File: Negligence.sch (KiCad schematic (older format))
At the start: 116 parts, among them J1 AVR-ISP-6, SW1 keyboard_parts_KEYSW, SW10 keyboard_parts_KEYSW, SW11 keyboard_parts_KEYSW, SW12 keyboard_parts_KEYSW, SW13 keyboard_parts_KEYSW, SW14 keyboard_parts_KEYSW, SW15 keyboard_parts_KEYSW, SW16 keyboard_parts_KEYSW, SW17 keyboard_parts_KEYSW, SW18 keyboard_parts_KEYSW, SW19 keyboard_parts_KEYSW, SW2 keyboard_parts_KEYSW, SW20 keyboard_parts_KEYSW, SW21 keyboard_parts_KEYSW, SW22 keyboard_parts_KEYSW, SW23 keyboard_parts_KEYSW, SW24 keyboard_parts_KEYSW, SW25 keyboard_parts_KEYSW, SW26 keyboard_parts_KEYSW, SW27 keyboard_parts_KEYSW, SW28 keyboard_parts_KEYSW, SW29 keyboard_parts_KEYSW, SW3 keyboard_parts_KEYSW, SW30 keyboard_parts_KEYSW, SW31 keyboard_parts_KEYSW, SW32 keyboard_parts_KEYSW, SW33 keyboard_parts_KEYSW, SW34 keyboard_parts_KEYSW, SW35 keyboard_parts_KEYSW, SW36 keyboard_parts_KEYSW, SW37 keyboard_parts_KEYSW, SW38 keyboard_parts_KEYSW, SW39 keyboard_parts_KEYSW, SW4 keyboard_parts_KEYSW, SW40 keyboard_parts_KEYSW, SW41 keyboard_parts_KEYSW, SW42 keyboard_parts_KEYSW, SW43 keyboard_parts_KEYSW, SW44 keyboard_parts_KEYSW, SW45 keyboard_parts_KEYSW, SW46 keyboard_parts_KEYSW, SW47 RESET, SW48 BOOT, SW5 keyboard_parts_KEYSW, SW6 keyboard_parts_KEYSW, SW7 keyboard_parts_KEYSW, SW8 keyboard_parts_KEYSW, SW9 keyboard_parts_KEYSW, U1 ATmega328P-PU, Y1 16MHz

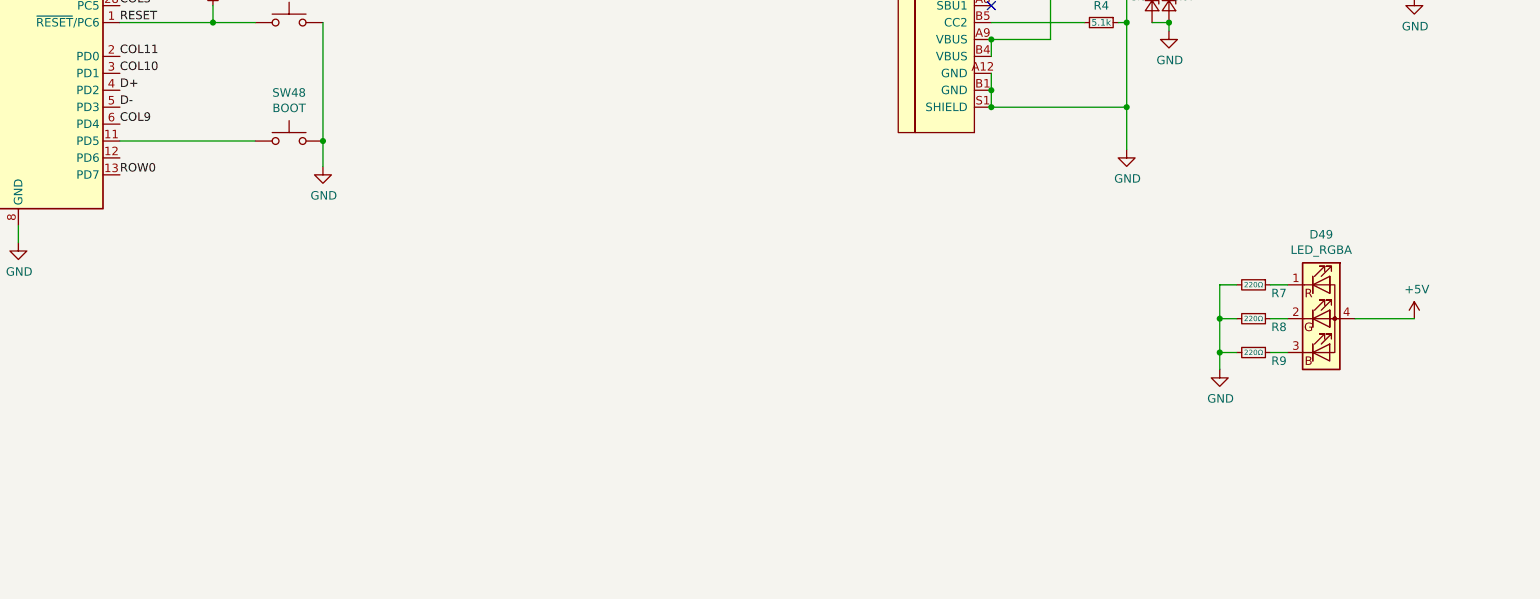
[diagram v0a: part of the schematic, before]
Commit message: Add addressable led
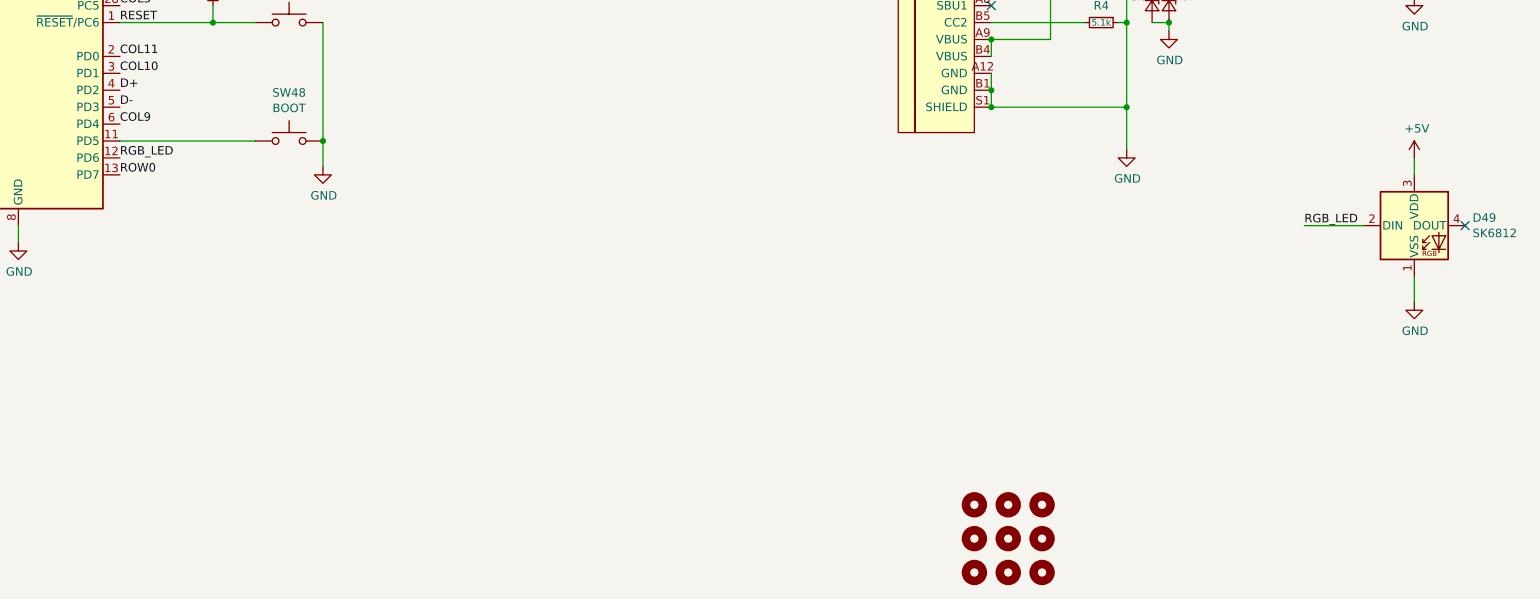
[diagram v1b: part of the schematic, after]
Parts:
- removed D49: LED_RGBA, LED_THT:LED_D5.0mm-4_RGB, symbol Device:LED_RGBA
- removed R7, R8, R9: 220Ω, cftkb:R_Axial_DIN0204_L3.6mm_D1.6mm_P7.62mm_Horizontal, symbol Device:R_Small
- added D49: SK6812, LED_SMD:LED_SK6812_PLCC4_5.0x5.0mm_P3.2mm, symbol LED:SK6812
- added H1, H2, H3, H4, H5, H6, H7, H8, H9: MountingHole, MountingHole:MountingHole_2.2mm_M2, symbol Mechanical:MountingHole
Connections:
- net +5V: now also D49.3 (VDD)
- net GND: now also D49.1 (VSS)
- net RGB_LED: now reaches U1.12 (PD6)
- net RGB_LED: now also D49.2 (DIN)
- no-connect marks 3 -> 4
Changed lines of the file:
@@
 Text Label 6900 7450 0    50   ~ 0
 ROW0
+Text Label 13900 7750 0    50   ~ 0
+RGB_LED
+Wire Wire Line
+	13900 7750 14250 7750
 $Comp
-L power:+5V #PWR016
-U 1 1 5F6FE958
-P 14550 8300
-F 0 "#PWR016" H 14550 8150 50  0001 C CNN
-F 1 "+5V" H 14565 8473 50  0000 C CNN
-F 2 "" H 14550 8300 50  0001 C CNN
-F 3 "" H 14550 8300 50  0001 C CNN
-	1    14550 8300
+L power:GND #PWR016
+U 1 1 5DEC76FA
+P 14550 8200
+F 0 "#PWR016" H 14550 7950 50  0001 C CNN
+F 1 "GND" H 14555 8027 50  0000 C CNN
+F 2 "" H 14550 8200 50  0001 C CNN
+F 3 "" H 14550 8200 50  0001 C CNN
+	1    14550 8200
 	1    0    0    -1
 $EndComp
 Wire Wire Line
-	14200 8300 14550 8300
+	14550 8050 14550 8200
+NoConn ~ 14850 7750
+Text Label 6900 7350 0    50   ~ 0
+RGB_LED
 $Comp
-L Device:R_Small R9
-U 1 1 5F717CE0
-P 13600 8500
-F 0 "R9" V 13650 8650 50  0000 C CNN
-F 1 "220Ω" V 13600 8500 31  0000 C CNN
-F 2 "cftkb:R_Axial_DIN0204_L3.6mm_D1.6mm_P7.62mm_Horizontal" H 13600 8500 50  0001 C CNN
-F 3 "~" H 13600 8500 50  0001 C CNN
-	1    13600 8500
-	0    1    1    0
-$EndComp
-Wire Wire Line
-	13700 8500 13800 8500
-$Comp
-L Device:R_Small R8
-U 1 1 5F78099C
-P 13600 8300
-F 0 "R8" V 13650 8450 50  0000 C CNN
-F 1 "220Ω" V 13600 8300 31  0000 C CNN
-F 2 "cftkb:R_Axial_DIN0204_L3.6mm_D1.6mm_P7.62mm_Horizontal" H 13600 8300 50  0001 C CNN
-F 3 "~" H 13600 8300 50  0001 C CNN
-	1    13600 8300
-	0    1    1    0
-$EndComp
-$Comp
-L Device:R_Small R7
-U 1 1 5F780E79
-P 13600 8100
-F 0 "R7" V 13650 8250 50  0000 C CNN
-F 1 "220Ω" V 13600 8100 31  0000 C CNN
-F 2 "cftkb:R_Axial_DIN0204_L3.6mm_D1.6mm_P7.62mm_Horizontal" H 13600 8100 50  0001 C CNN
-F 3 "~" H 13600 8100 50  0001 C CNN
-	1    13600 8100
-	0    1    1    0
-$EndComp
-Wire Wire Line
-	13700 8100 13800 8100
-Wire Wire Line
-	13700 8300 13800 8300
-$Comp
-L power:GND #PWR015
-U 1 1 5F7AE110
-P 13400 8600
-F 0 "#PWR015" H 13400 8350 50  0001 C CNN
-F 1 "GND" H 13405 8427 50  0000 C CNN
-F 2 "" H 13400 8600 50  0001 C CNN
-F 3 "" H 13400 8600 50  0001 C CNN
-	1    13400 8600
+L LED:SK6812 D49
+U 1 1 5DEAB758
+P 14550 7750
+F 0 "D49" H 14894 7796 50  0000 L CNN
+F 1 "SK6812" H 14894 7705 50  0000 L CNN
+F 2 "LED_SMD:LED_SK6812_PLCC4_5.0x5.0mm_P3.2mm" H 14600 7450 50  0001 L TNN
+F 3 "https://cdn-shop.adafruit.com/product-files/1138/SK6812+LED+datasheet+.pdf" H 14650 7375 50  0001 L TNN
+	1    14550 7750
 	1    0    0    -1
 $EndComp
 Wire Wire Line
-	13400 8600 13400 8500
-Wire Wire Line
-	13400 8100 13500 8100
-Wire Wire Line
-	13500 8300 13400 8300
-Connection ~ 13400 8300
-Wire Wire Line
-	13400 8300 13400 8100
-Wire Wire Line
-	13500 8500 13400 8500
-Connection ~ 13400 8500
-Wire Wire Line
-	13400 8500 13400 8300
+	14550 7350 14550 7450
 $Comp
-L Device:LED_RGBA D49
-U 1 1 5F803903
-P 14000 8300
-F 0 "D49" H 14000 8797 50  0000 C CNN
-F 1 "LED_RGBA" H 14000 8706 50  0000 C CNN
-F 2 "LED_THT:LED_D5.0mm-4_RGB" H 14000 8250 50  0001 C CNN
-F 3 "~" H 14000 8250 50  0001 C CNN
-	1    14000 8300
+L power:+5V #PWR015
+U 1 1 5DF0A5B4
+P 14550 7350
+F 0 "#PWR015" H 14550 7200 50  0001 C CNN
+F 1 "+5V" H 14565 7523 50  0000 C CNN
+F 2 "" H 14550 7350 50  0001 C CNN
+F 3 "" H 14550 7350 50  0001 C CNN
+	1    14550 7350
 	1    0    0    -1
 $EndComp
+$Comp
+L Mechanical:MountingHole H3
+U 1 1 5E0427A4
+P 11950 9800
+F 0 "H3" H 12050 9846 50  0001 L CNN
+F 1 "MountingHole" H 12050 9800 50  0001 L CNN
+F 2 "MountingHole:MountingHole_2.2mm_M2" H 11950 9800 50  0001 C CNN
+F 3 "~" H 11950 9800 50  0001 C CNN
+	1    11950 9800
+	1    0    0    -1
+$EndComp
+$Comp
+L Mechanical:MountingHole H6
+U 1 1 5E04AB55
+P 12150 9800
+F 0 "H6" H 12250 9846 50  0001 L CNN
+F 1 "MountingHole" H 12250 9800 50  0001 L CNN
+F 2 "MountingHole:MountingHole_2.2mm_M2" H 12150 9800 50  0001 C CNN
+F 3 "~" H 12150 9800 50  0001 C CNN
+	1    12150 9800
+	1    0    0    -1
+$EndComp
+$Comp
+L Mechanical:MountingHole H9
+U 1 1 5E04B0DD
+P 12350 9800
+F 0 "H9" H 12450 9846 50  0001 L CNN
+F 1 "MountingHole" H 12450 9800 50  0001 L CNN
+F 2 "MountingHole:MountingHole_2.2mm_M2" H 12350 9800 50  0001 C CNN
+F 3 "~" H 12350 9800 50  0001 C CNN
+	1    12350 9800
+	1    0    0    -1
+$EndComp
+$Comp
+L Mechanical:MountingHole H2
+U 1 1 5E04B3C2
+P 11950 9600
+F 0 "H2" H 12050 9646 50  0001 L CNN
+F 1 "MountingHole" H 12050 9600 50  0001 L CNN
+F 2 "MountingHole:MountingHole_2.2mm_M2" H 11950 9600 50  0001 C CNN
+F 3 "~" H 11950 9600 50  0001 C CNN
+	1    11950 9600
+	1    0    0    -1
+$EndComp
+$Comp
+L Mechanical:MountingHole H1
+U 1 1 5E04B4F4
+P 11950 9400
+F 0 "H1" H 12050 9446 50  0001 L CNN
+F 1 "MountingHole" H 12050 9400 50  0001 L CNN
+F 2 "MountingHole:MountingHole_2.2mm_M2" H 11950 9400 50  0001 C CNN
+F 3 "~" H 11950 9400 50  0001 C CNN
+	1    11950 9400
+	1    0    0    -1
+$EndComp
+$Comp
+L Mechanical:MountingHole H5
+U 1 1 5E04B833
+P 12150 9600
+F 0 "H5" H 12250 9646 50  0001 L CNN
+F 1 "MountingHole" H 12250 9600 50  0001 L CNN
+F 2 "MountingHole:MountingHole_2.2mm_M2" H 12150 9600 50  0001 C CNN
+F 3 "~" H 12150 9600 50  0001 C CNN
+	1    12150 9600
+	1    0    0    -1
+$EndComp
+$Comp
+L Mechanical:MountingHole H4
+U 1 1 5E04BE24
+P 12150 9400
+F 0 "H4" H 12250 9446 50  0001 L CNN
+F 1 "MountingHole" H 12250 9400 50  0001 L CNN
+F 2 "MountingHole:MountingHole_2.2mm_M2" H 12150 9400 50  0001 C CNN
+F 3 "~" H 12150 9400 50  0001 C CNN
+	1    12150 9400
+	1    0    0    -1
+$EndComp
+$Comp
+L Mechanical:MountingHole H8
+U 1 1 5E04BFB0
+P 12350 9600
+F 0 "H8" H 12450 9646 50  0001 L CNN
+F 1 "MountingHole" H 12450 9600 50  0001 L CNN
+F 2 "MountingHole:MountingHole_2.2mm_M2" H 12350 9600 50  0001 C CNN
+F 3 "~" H 12350 9600 50  0001 C CNN
+	1    12350 9600
+	1    0    0    -1
+$EndComp
+$Comp
+L Mechanical:MountingHole H7
+U 1 1 5E04C0C4
+P 12350 9400
+F 0 "H7" H 12450 9446 50  0001 L CNN
+F 1 "MountingHole" H 12450 9400 50  0001 L CNN
+F 2 "MountingHole:MountingHole_2.2mm_M2" H 12350 9400 50  0001 C CNN
+F 3 "~" H 12350 9400 50  0001 C CNN
+	1    12350 9400
+	1    0    0    -1
+$EndComp

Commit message: various updates
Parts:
- R1, R2, R3, R4, R5, R6: footprint cftkb:R_Axial_DIN0204_L3.6mm_D1.6mm_P7.62mm_Horizontal -> Resistor_THT:R_Axial_DIN0204_L3.6mm_D1.6mm_P5.08mm_Horizontal
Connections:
- net BOOT: now reaches SW48.1, U1.11 (PD5)
- net CC1: now reaches R3.2, USB1.A5 (CC1)
- net CC2: now reaches R4.2, USB1.B5 (CC2)
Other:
- moved on the sheet: C1, C2, C3, C4, C5, D1, D10, D11, D12, D13, D14, D15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
